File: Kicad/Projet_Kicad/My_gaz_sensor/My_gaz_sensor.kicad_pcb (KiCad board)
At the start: 2 copper layers, 134.6 x 64.8 mm, 21 parts, among them P1 Power, P2 Analog, P3 Digital, P4 Digital, P5 CONN_01X01, P6 CONN_01X01, P7 CONN_01X01, P8 CONN_01X01, U1 LTC1050, U11 RN2483A

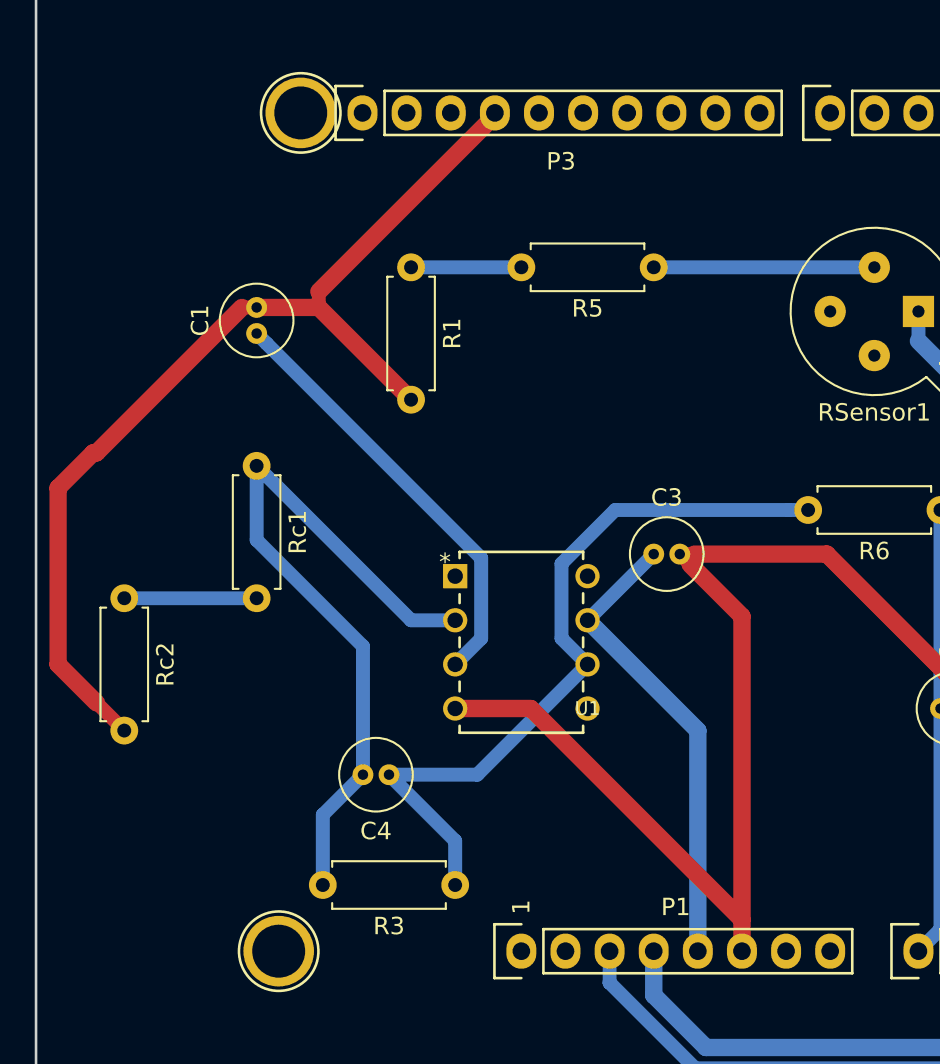
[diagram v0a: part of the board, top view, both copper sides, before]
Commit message: Refactor valeur C4
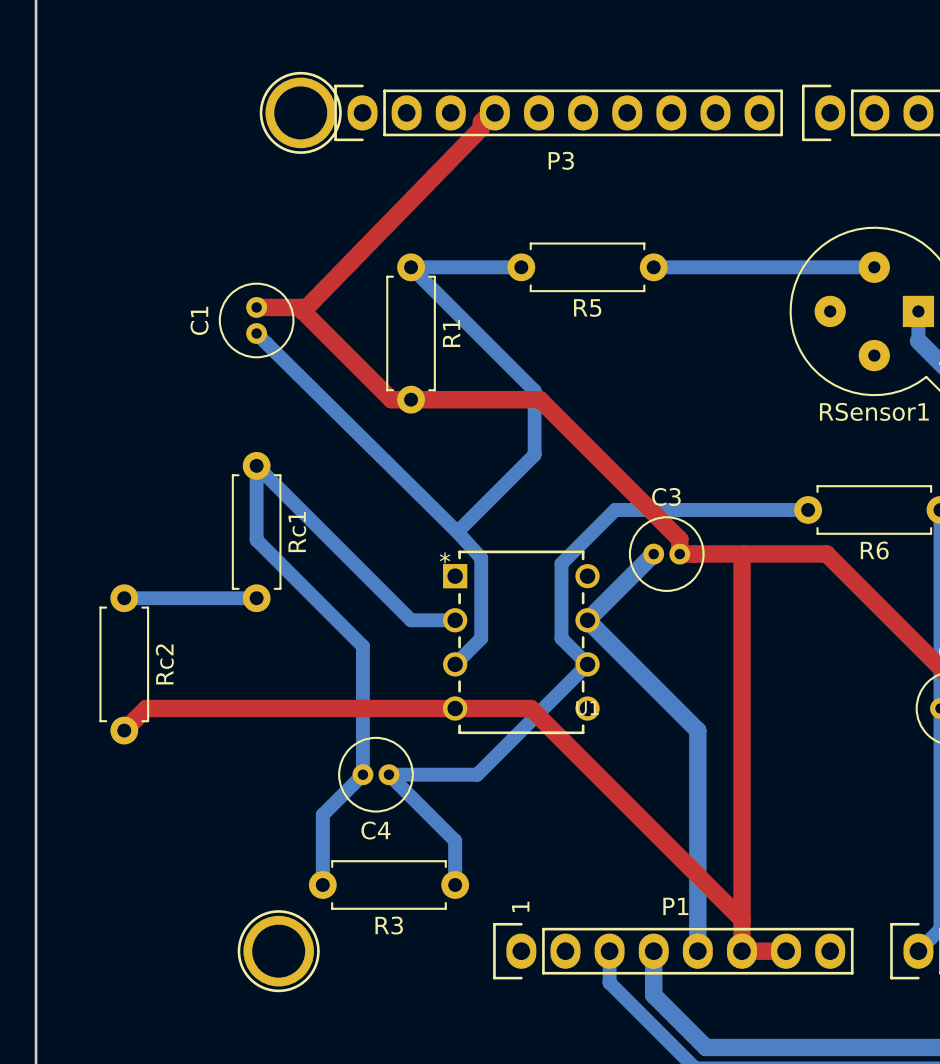
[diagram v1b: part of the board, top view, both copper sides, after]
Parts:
- C4: value 100n -> 1μ
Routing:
- net Net-(C1-Pad1): track 31.4 -> 51.4 mm
- net GND: track 158.3 -> 166.3 mm
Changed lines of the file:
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@@
     (thickness 1.6)
     (drawings 25)
-    (tracks 82)
+    (tracks 91)
     (zones 0)
     (modules 21)
@@
       (effects (font (size 1 1) (thickness 0.15)))
     )
-    (fp_text value 100n (at 0.75 3.25) (layer F.Fab)
+    (fp_text value 1μ (at 0.75 3.25) (layer F.Fab)
       (effects (font (size 1 1) (thickness 0.15)))
     )
@@
   (segment (start 207.518 83.85) (end 198.15 93.218) (width 0.8) (layer B.Cu) (net 20))
   (segment (start 207.518 80.645) (end 207.518 83.85) (width 0.8) (layer B.Cu) (net 20))
-  (segment (start 142.748 104.775) (end 146.558 100.965) (width 0.8) (layer B.Cu) (net 45))
   (segment (start 146.558 126.365) (end 146.558 123.825) (width 1) (layer B.Cu) (net 28))
   (segment (start 188.468 108.936) (end 188.468 116.205) (width 1) (layer B.Cu) (net 28))
@@
   (segment (start 191.1835 106.2205) (end 188.468 108.936) (width 1) (layer B.Cu) (net 28))
   (segment (start 194.026 103.378) (end 191.1835 106.2205) (width 1) (layer B.Cu) (net 28))
-  (segment (start 136.626501 101.193501) (end 124.297999 88.864999) (width 0.8) (layer B.Cu) (net 31))
   (segment (start 136.626501 105.816499) (end 136.626501 101.193501) (width 0.8) (layer B.Cu) (net 31))
   (segment (start 124.297999 88.864999) (end 123.698 88.265) (width 0.8) (layer B.Cu) (net 31))
   (segment (start 135.128 107.315) (end 136.626501 105.816499) (width 0.8) (layer B.Cu) (net 31))
   (segment (start 138.938 84.455) (end 132.588 84.455) (width 0.8) (layer B.Cu) (net 31))
+  (segment (start 132.588 84.455) (end 139.7 91.567) (width 0.8) (layer B.Cu) (net 31))
+  (segment (start 139.7 91.567) (end 139.7 95.25) (width 0.8) (layer B.Cu) (net 31))
+  (segment (start 139.7 95.25) (end 135.255 99.695) (width 0.8) (layer B.Cu) (net 31))
+  (segment (start 136.626501 101.193501) (end 135.255 99.695) (width 0.8) (layer B.Cu) (net 31))
+  (segment (start 135.255 99.695) (end 124.297999 88.864999) (width 0.8) (layer B.Cu) (net 31))
   (segment (start 135.128 120.015) (end 135.128 117.475) (width 0.8) (layer B.Cu) (net 32))
   (segment (start 135.128 117.475) (end 131.318 113.665) (width 0.8) (layer B.Cu) (net 32))
@@
   (segment (start 146.558 84.455) (end 159.258 84.455) (width 0.8) (layer B.Cu) (net 36))
   (segment (start 116.078 103.505) (end 123.698 103.505) (width 0.8) (layer B.Cu) (net 37))
-  (segment (start 148.657999 101.564999) (end 148.058 100.965) (width 0.8) (layer F.Cu) (net 44))
-  (segment (start 151.638 104.545) (end 148.657999 101.564999) (width 1) (layer F.Cu) (net 44))
-  (segment (start 151.638 123.825) (end 151.638 104.545) (width 1) (layer F.Cu) (net 44))
-  (segment (start 148.906528 100.965) (end 148.058 100.965) (width 0.8) (layer F.Cu) (net 44))
-  (segment (start 156.526528 100.965) (end 148.906528 100.965) (width 1) (layer F.Cu) (net 44))
+  (segment (start 148.906528 100.965) (end 148.058 100.965) (width 1) (layer F.Cu) (net 44))
   (segment (start 164.568 109.006472) (end 156.526528 100.965) (width 1) (layer F.Cu) (net 44))
   (segment (start 164.568 109.855) (end 164.568 109.006472) (width 0.8) (layer F.Cu) (net 44))
   (segment (start 165.965 108.458) (end 164.568 109.855) (width 1) (layer F.Cu) (net 44))
   (segment (start 196.088 108.458) (end 165.965 108.458) (width 1) (layer F.Cu) (net 44))
-  (segment (start 127.278 86.765) (end 123.698 86.765) (width 1) (layer F.Cu) (net 44))
-  (segment (start 132.588 92.075) (end 127.278 86.765) (width 1) (layer F.Cu) (net 44))
-  (segment (start 127.278 85.8534) (end 127.278 86.765) (width 0.8) (layer F.Cu) (net 44))
-  (segment (start 137.414 75.7174) (end 127.278 85.8534) (width 1) (layer F.Cu) (net 44))
-  (segment (start 137.414 75.565) (end 137.414 75.7174) (width 0.8) (layer F.Cu) (net 44))
-  (segment (start 122.849472 86.765) (end 123.698 86.765) (width 0.8) (layer F.Cu) (net 44))
-  (segment (start 114.477999 95.136473) (end 122.849472 86.765) (width 1) (layer F.Cu) (net 44))
-  (segment (start 116.078 111.125) (end 114.477999 109.524999) (width 0.8) (layer F.Cu) (net 44))
-  (segment (start 151.638 122.009) (end 151.638 123.825) (width 0.8) (layer F.Cu) (net 44))
+  (segment (start 151.638 122.009) (end 151.638 123.825) (width 1) (layer F.Cu) (net 44))
   (segment (start 139.484 109.855) (end 151.638 122.009) (width 1) (layer F.Cu) (net 44))
   (segment (start 135.128 109.855) (end 139.484 109.855) (width 1) (layer F.Cu) (net 44))
-  (segment (start 114.286527 95.136473) (end 112.268 97.155) (width 1) (layer F.Cu) (net 44))
-  (segment (start 114.477999 95.136473) (end 114.286527 95.136473) (width 1) (layer F.Cu) (net 44))
-  (segment (start 112.268 97.155) (end 112.268 107.315) (width 1) (layer F.Cu) (net 44))
-  (segment (start 112.268 107.315) (end 114.477999 109.524999) (width 1) (layer F.Cu) (net 44))
+  (segment (start 154.178 123.825) (end 151.638 123.825) (width 1) (layer F.Cu) (net 44))
+  (segment (start 151.638 101.092) (end 151.765 100.965) (width 1) (layer F.Cu) (net 44))
+  (segment (start 151.638 122.009) (end 151.638 101.092) (width 1) (layer F.Cu) (net 44))
+  (segment (start 156.526528 100.965) (end 151.765 100.965) (width 1) (layer F.Cu) (net 44))
+  (segment (start 151.765 100.965) (end 148.906528 100.965) (width 1) (layer F.Cu) (net 44))
+  (segment (start 133.71937 92.075) (end 132.588 92.075) (width 1) (layer F.Cu) (net 44))
+  (segment (start 140.016528 92.075) (end 133.71937 92.075) (width 1) (layer F.Cu) (net 44))
+  (segment (start 148.058 100.116472) (end 140.016528 92.075) (width 1) (layer F.Cu) (net 44))
+  (segment (start 148.058 100.965) (end 148.058 100.116472) (width 1) (layer F.Cu) (net 44))
+  (segment (start 124.546528 86.765) (end 123.698 86.765) (width 1) (layer F.Cu) (net 44))
+  (segment (start 126.320521 86.765) (end 124.546528 86.765) (width 1) (layer F.Cu) (net 44))
+  (segment (start 136.63761 76.08739) (end 136.63761 76.447911) (width 1) (layer F.Cu) (net 44))
+  (segment (start 137.16 75.565) (end 136.63761 76.08739) (width 1) (layer F.Cu) (net 44))
+  (segment (start 137.414 75.565) (end 137.16 75.565) (width 1) (layer F.Cu) (net 44))
+  (segment (start 126.37663 86.995) (end 126.365 86.995) (width 1) (layer F.Cu) (net 44))
+  (segment (start 131.45663 92.075) (end 126.37663 86.995) (width 1) (layer F.Cu) (net 44))
+  (segment (start 132.588 92.075) (end 131.45663 92.075) (width 1) (layer F.Cu) (net 44))
+  (segment (start 136.63761 76.447911) (end 126.365 86.995) (width 1) (layer F.Cu) (net 44))
+  (segment (start 126.365 86.995) (end 126.320521 86.765) (width 1) (layer F.Cu) (net 44))
+  (segment (start 117.348 109.855) (end 116.078 111.125) (width 1) (layer F.Cu) (net 44))
+  (segment (start 135.128 109.855) (end 117.348 109.855) (width 1) (layer F.Cu) (net 44))
+  (segment (start 142.748 104.775) (end 146.558 100.965) (width 1) (layer B.Cu) (net 45))
   (segment (start 149.098 111.125) (end 142.748 104.775) (width 1) (layer B.Cu) (net 45))
   (segment (start 149.098 123.825) (end 149.098 111.125) (width 1) (layer B.Cu) (net 45))
